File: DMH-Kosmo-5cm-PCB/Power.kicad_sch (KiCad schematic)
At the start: 14 parts, among them J0 Conn_01x01, J100 IDC_02x05, J101 IDC_02x08

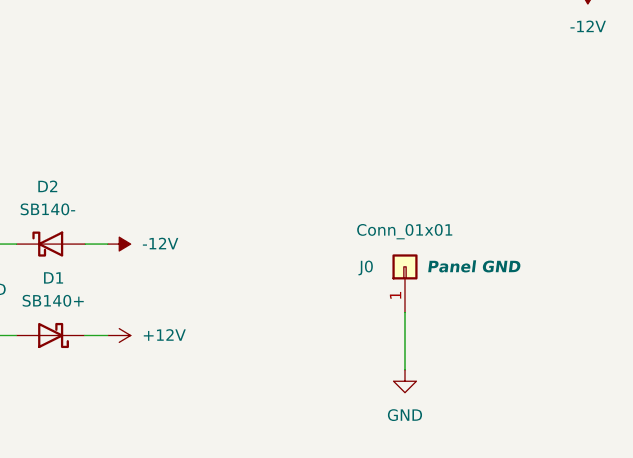
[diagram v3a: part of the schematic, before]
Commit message: Added initial jacks and connectors to PCBs
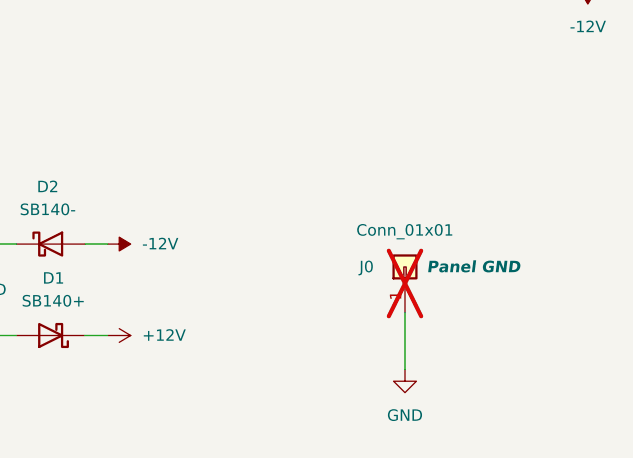
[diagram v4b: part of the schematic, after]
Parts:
- J0: now not fitted; now left out of the parts list
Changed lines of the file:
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@@
 		(unit 1)
 		(exclude_from_sim no)
-		(in_bom yes)
+		(in_bom no)
 		(on_board yes)
-		(dnp no)
+		(dnp yes)
 		(property "Reference" "J0"
 			(at 147.32 177.8 90)
